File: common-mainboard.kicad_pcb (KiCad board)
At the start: 2 copper layers, 72.4 x 48.3 mm, 82 parts, among them J1 SIM_Card, J2 RSP-122811-01, J3 Conn_01x02_Female, Q1 DTC043ZEB, Q2 DTC043ZEB, Q3 DTC043ZEB, SW1 SW_Push, SW2 SW_Push, U1 ATSAMD21J18A-M, U10 STC3100IQT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

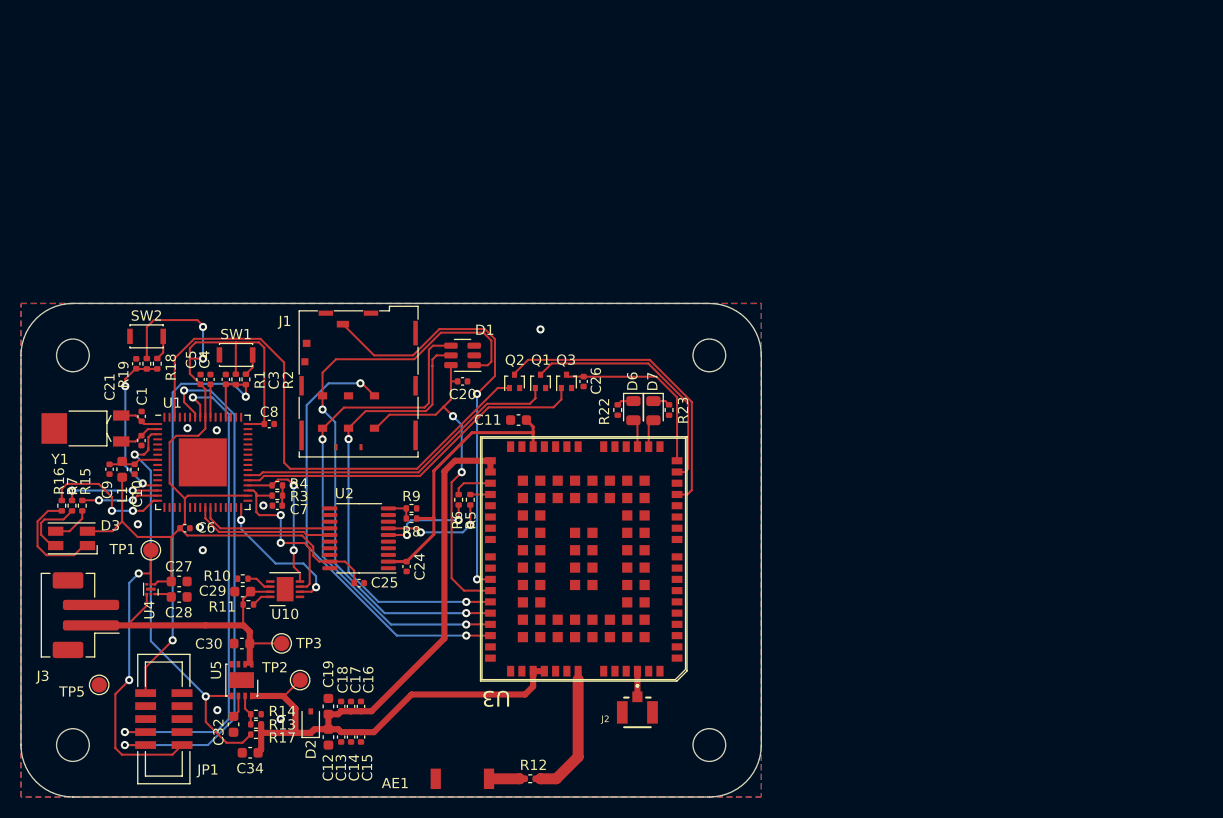
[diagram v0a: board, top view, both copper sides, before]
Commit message: eg915u: modified page layout, added USB upgrade support (sch + pcb)
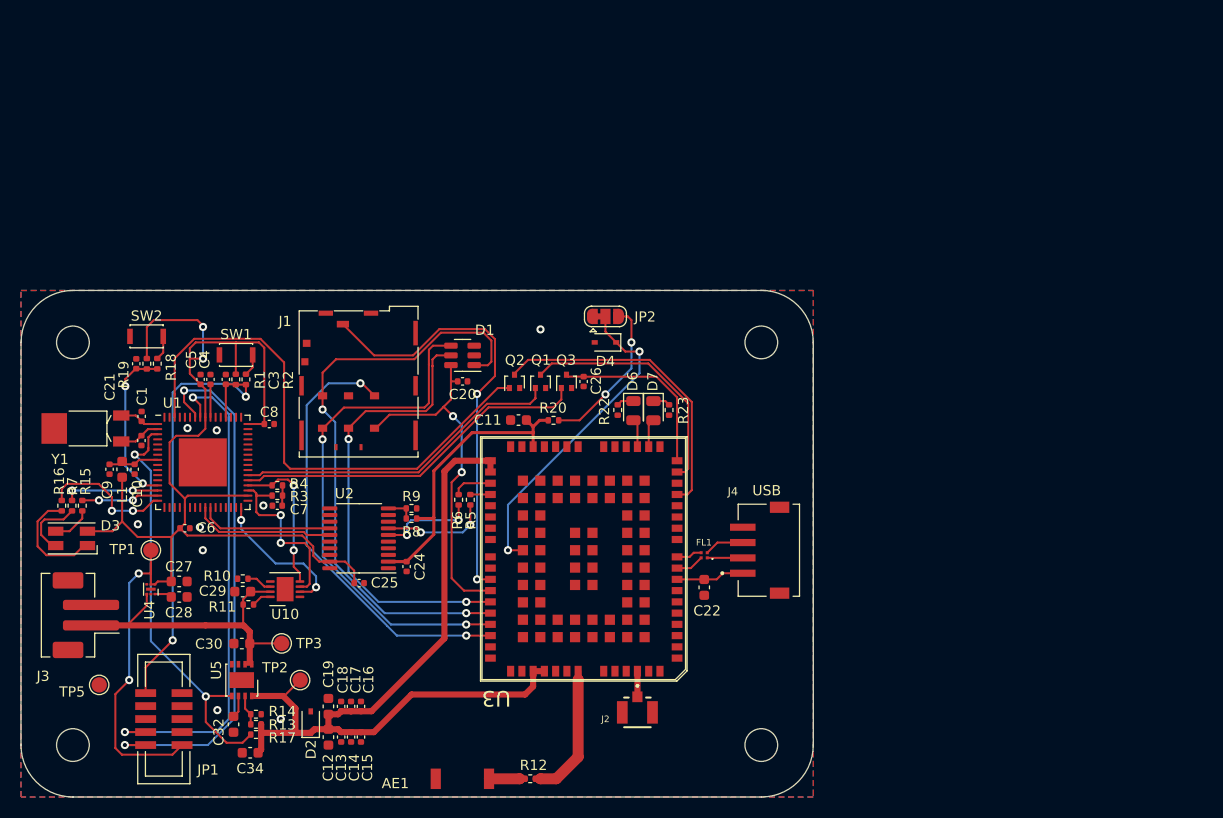
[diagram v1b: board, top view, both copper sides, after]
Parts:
- added C22: 1uF_10V, Capacitor_SMD:C_0603_1608Metric, F.Cu at (137.9, 130.6)
- added D4: SD05_SOD323, Diode_SMD:D_SOD-323, F.Cu at (128.3, 106.7)
- added FL1: DLM0NSN900HY2D, DLM0NSN900HY2D:FIL_DLM0NSN900HY2D, F.Cu at (137.9, 127.5)
- added J4: S4B-ZR-SM4A-TF(LF)(SN), S4B-ZR-SM4A-TF_LF__SN_:JST_S4B-ZR-SM4A-TF(LF)(SN), F.Cu at (141.7, 127.0)
- added JP2: SolderJumper_3_Bridged12, Jumper:SolderJumper-3_P1.3mm_Bridged12_RoundedPad1.0x1.5mm, F.Cu at (128.3, 104.1)
- added R20: 4k7, Resistor_SMD:R_0402_1005Metric, F.Cu at (123.2, 114.3)
- moved H3 5.24 mm to (143.5, 106.7)
- moved H2 5.08 mm to (143.5, 146.1)
- moved H4 1.27 mm to (76.2, 106.7)
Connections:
- U3 pad 10: unconnected-(U3-Pad10) -> Net-(FL1-Pad3)
- U3 pad 75: unconnected-(U3-Pad75) -> USB_BOOT
- U3 pad 8: unconnected-(U3-Pad8) -> USB_VBUS
- U3 pad 9: unconnected-(U3-Pad9) -> Net-(FL1-Pad2)
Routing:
- net USB_BOOT: track 0.00 -> 31.8 mm, vias 0 -> 2
- net Net-(JP2-Pad3): track 0.00 -> 15.3 mm, vias 0 -> 2
- net USB_VBUS: track 0.00 -> 6.67 mm
- net USB_DM: track 0.00 -> 3.88 mm
- net USB_DP: track 0.00 -> 3.47 mm
- net Net-(FL1-Pad2): track 0.00 -> 2.77 mm
- net Net-(FL1-Pad3): track 0.00 -> 2.52 mm
- net VDD_EXT: track 27.8 -> 29.5 mm
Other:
- board size 72.4 x 48.3 mm -> 77.5 x 49.5 mm
- board text added: "USB"

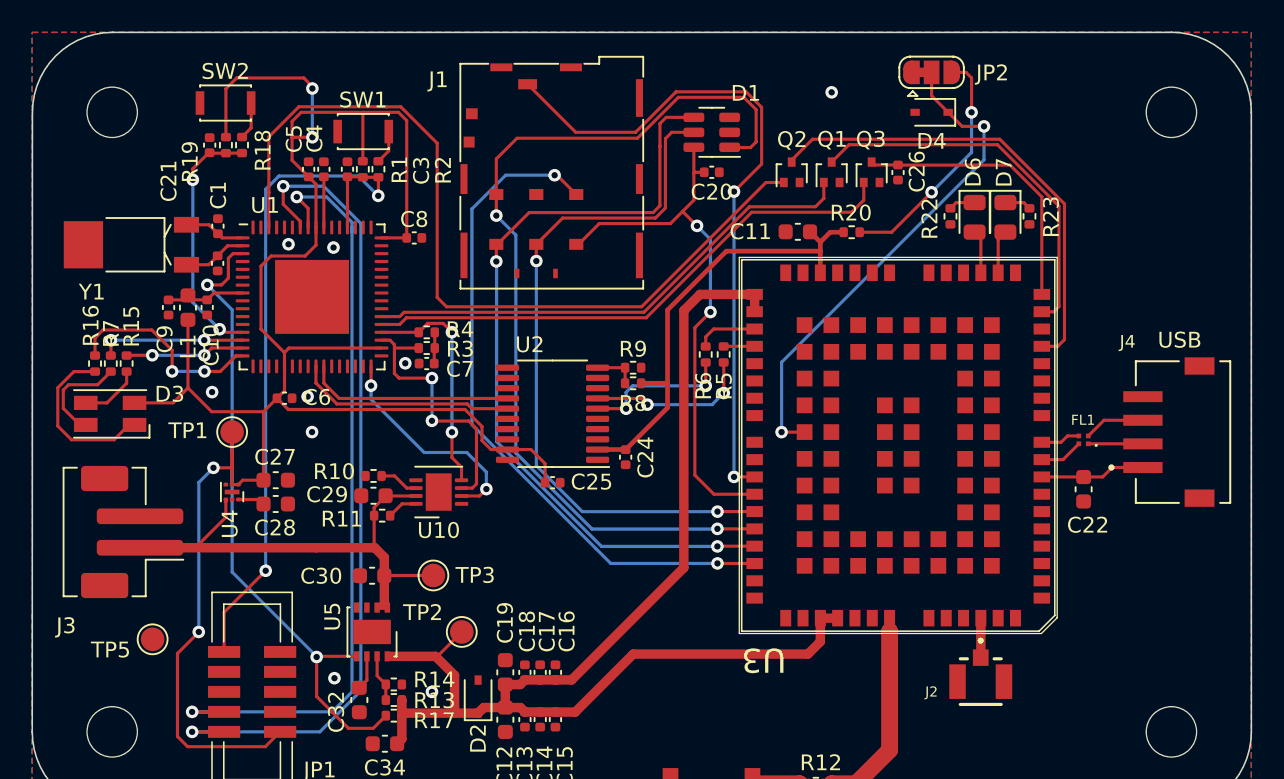
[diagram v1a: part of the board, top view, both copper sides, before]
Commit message: added UART flow control pins CTS and RTS
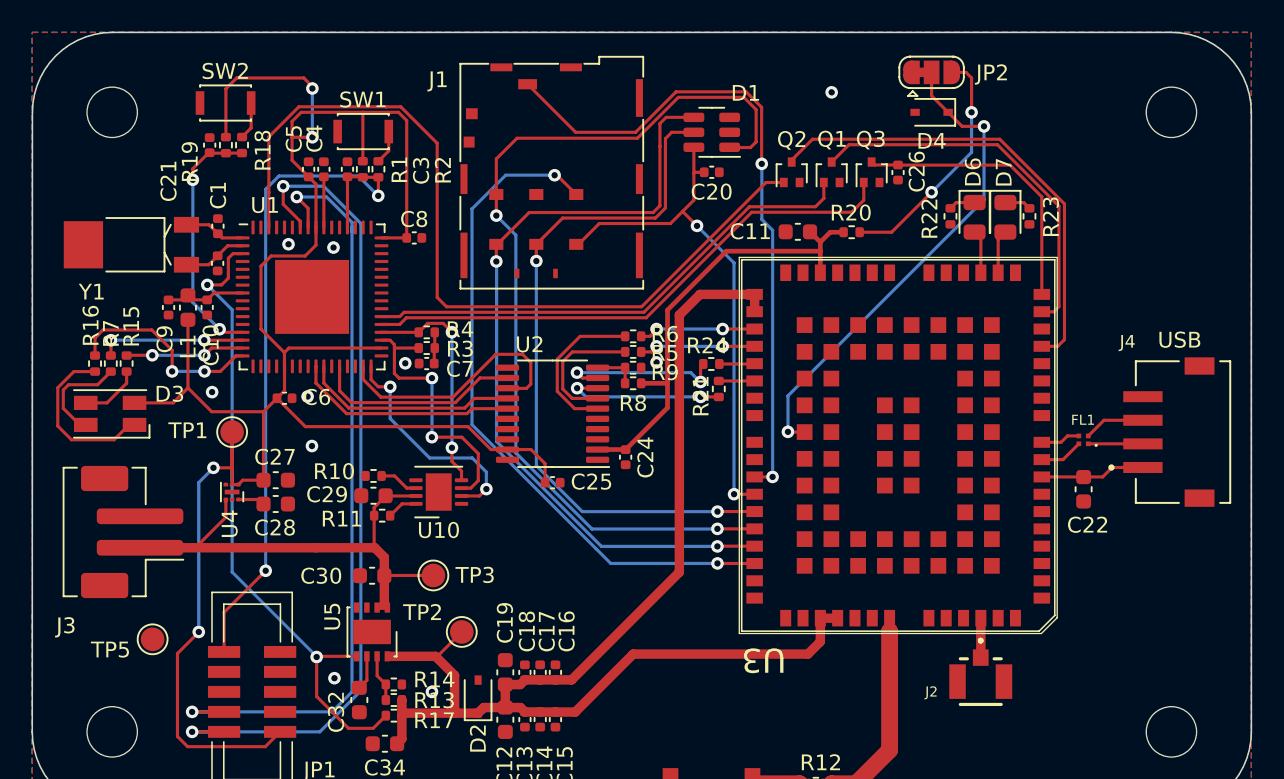
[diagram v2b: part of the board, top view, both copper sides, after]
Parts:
- added R21: 0R, Resistor_SMD:R_0402_1005Metric, F.Cu at (114.7, 124.3)
- added R24: 0R, Resistor_SMD:R_0402_1005Metric, F.Cu at (114.3, 122.7)
- moved R5 5.75 mm to (109.3, 121.9), turned to 180 degrees
- moved R6 4.75 mm to (109.3, 120.9), turned to 180 degrees
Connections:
- U1 pad 28: unconnected-(U1-Pad28) -> UC_DCE_CTS
- U1 pad 31: unconnected-(U1-Pad31) -> UC_DCE_RTS
- U2 pad 12: unconnected-(U2-Pad12) -> UC_DCE_CTS
- U2 pad 13: unconnected-(U2-Pad13) -> UC_DCE_RTS
- U2 pad 8: unconnected-(U2-Pad8) -> DCE_RTS
- U2 pad 9: unconnected-(U2-Pad9) -> DCE_CTS
- U3 pad 36: unconnected-(U3-Pad36) -> Net-(U3-Pad36)
- U3 pad 37: unconnected-(U3-Pad37) -> Net-(U3-Pad37)
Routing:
- net UC_DCE_RTS: track 0.00 -> 16.3 mm
- net UC_DCE_CTS: track 0.00 -> 13.2 mm
- net DCE_CTS: track 0.00 -> 10.8 mm, vias 0 -> 2
- net DCE_RTS: track 0.00 -> 10.5 mm, vias 0 -> 2
- net Net-(R5-Pad1): track 1.97 -> 7.40 mm, vias 0 -> 2
- net Net-(R6-Pad1): track 3.92 -> 7.50 mm, vias 0 -> 2
- net Net-(U3-Pad37): track 0.00 -> 2.28 mm
- net Net-(U3-Pad36): track 0.00 -> 2.25 mm
- net DCE_TX: track 10.4 -> 8.43 mm, vias 2 -> 0
- net USIM1_VDD: track 34.9 -> 33.3 mm
- net USIM1_DET: track 43.1 -> 42.5 mm
- net USB_BOOT: track 31.8 -> 31.3 mm
- net +3V3: track 136.0 -> 135.5 mm
- net UC_DCE_TX: track 13.1 -> 13.7 mm
- net DCE_RX: track 9.57 -> 9.97 mm, vias 2 -> 0
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
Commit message: added test point for VDD_EXT
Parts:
- added TP4: VDD_EXT, TestPoint:TestPoint_Pad_D1.5mm, F.Cu at (109.4, 131.4)
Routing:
- net VDD_EXT: track 29.5 -> 35.2 mm
- net GNDREF: vias 10 -> 13
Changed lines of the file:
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@@
   (net 186 "UC_DCE_CTS")
   (net 187 "UC_DCE_RTS")
+  (footprint "TestPoint:TestPoint_Pad_D1.5mm" (layer "F.Cu")
+    (at 109.350602 131.40853)
+    (descr "SMD pad as test Point, diameter 1.5mm")
+    (tags "test point SMD pad")
+    (property "Sheetfile" "lipo-power-supply.kicad_sch")
+    (property "Sheetname" "lipo-power-supply")
+    (attr exclude_from_pos_files)
+    (fp_text reference "TP4" (at 0 2.059945) (layer "F.SilkS")
+      (effects (font (size 1 1) (thickness 0.15)))
+    )
+    (fp_text value "VDD_EXT" (at 0 1.75) (layer "F.Fab")
+      (effects (font (size 1 1) (thickness 0.15)))
+    )
+    (fp_text user "${REFERENCE}" (at 0 -1.65) (layer "F.Fab")
+      (effects (font (size 1 1) (thickness 0.15)))
+    )
+    (fp_circle (center 0 0) (end 0 0.95) (layer "F.SilkS") (width 0.12) (fill none))
+    (fp_circle (center 0 0) (end 1.25 0) (layer "F.CrtYd") (width 0.05) (fill none))
+    (pad "1" smd circle (at 0 0) (size 1.5 1.5) (layers "F.Cu" "F.Mask")
+      (net 19 "VDD_EXT") (pinfunction "1") (pintype "passive"))
+  )
   (footprint "Resistor_SMD:R_0402_1005Metric" (layer "F.Cu")
     (at 120.915065 149.347023)
@@
   (via (at 96.52 143.51) (size 0.8) (drill 0.4) (layers "F.Cu" "B.Cu") (free) (net 2))
   (via (at 88.893866 127.886012) (size 0.8) (drill 0.4) (layers "F.Cu" "B.Cu") (free) (net 2))
+  (via (at 109.645313 126.36262) (size 0.8) (drill 0.4) (layers "F.Cu" "B.Cu") (free) (net 2))
   (via (at 90.263294 115.272692) (size 0.8) (drill 0.4) (layers "F.Cu" "B.Cu") (free) (net 2))
+  (via (at 114.3 119.38) (size 0.8) (drill 0.4) (layers "F.Cu" "B.Cu") (free) (net 2))
   (via (at 88.616178 124.74512) (size 0.8) (drill 0.4) (layers "F.Cu" "B.Cu") (free) (net 2))
+  (via (at 94.076408 112.56816) (size 0.8) (drill 0.4) (layers "F.Cu" "B.Cu") (free) (net 2))
   (via (at 121.92 105.41) (size 0.8) (drill 0.4) (layers "F.Cu" "B.Cu") (net 2))
   (via (at 82.55 124.46) (size 0.8) (drill 0.4) (layers "F.Cu" "B.Cu") (free) (net 2))
@@
   (segment (start 107.046544 128.110177) (end 108.821748 128.110177) (width 0.3) (layer "F.Cu") (net 19))
   (segment (start 111.490312 123.820192) (end 111.490312 119.240652) (width 0.3) (layer "F.Cu") (net 19))
-  (segment (start 108.827325 128.115754) (end 111.490312 125.452767) (width 0.3) (layer "F.Cu") (net 19))
   (segment (start 121.2 115.50329) (end 121.2 114.927745) (width 0.3) (layer "F.Cu") (net 19))
   (segment (start 109.933711 124.018434) (end 109.813685 123.898408) (width 0.3) (layer "F.Cu") (net 19))
+  (segment (start 108.827325 128.115754) (end 108.837885 128.105194) (width 0.3) (layer "F.Cu") (net 19))
   (segment (start 121.2 114.927745) (end 120.545187 114.272932) (width 0.3) (layer "F.Cu") (net 19))
   (segment (start 111.490312 119.240652) (end 115.227674 115.50329) (width 0.3) (layer "F.Cu") (net 19))
+  (segment (start 108.837885 128.105194) (end 111.466221 128.105194) (width 0.3) (layer "F.Cu") (net 19))
   (segment (start 121.2 116.875) (end 121.2 115.50329) (width 0.3) (layer "F.Cu") (net 19))
   (segment (start 111.412096 123.898408) (end 111.490312 123.820192) (width 0.3) (layer "F.Cu") (net 19))
+  (segment (start 109.350602 131.40853) (end 111.490312 129.26882) (width 0.3) (layer "F.Cu") (net 19))
   (segment (start 111.490312 125.452767) (end 111.490312 123.820192) (width 0.3) (layer "F.Cu") (net 19))
   (segment (start 109.813685 123.898408) (end 111.412096 123.898408) (width 0.3) (layer "F.Cu") (net 19))
   (segment (start 121.827745 114.3) (end 121.2 114.927745) (width 0.3) (layer "F.Cu") (net 19))
   (segment (start 115.227674 115.50329) (end 121.2 115.50329) (width 0.3) (layer "F.Cu") (net 19))
+  (segment (start 111.490312 129.26882) (end 111.490312 125.452767) (width 0.3) (layer "F.Cu") (net 19))
   (segment (start 105.626014 144.791793) (end 104.369914 144.791793) (width 0.6) (layer "F.Cu") (net 20))
   (segment (start 99.452509 144.86) (end 97.959126 144.86) (width 0.6) (layer "F.Cu") (net 20))

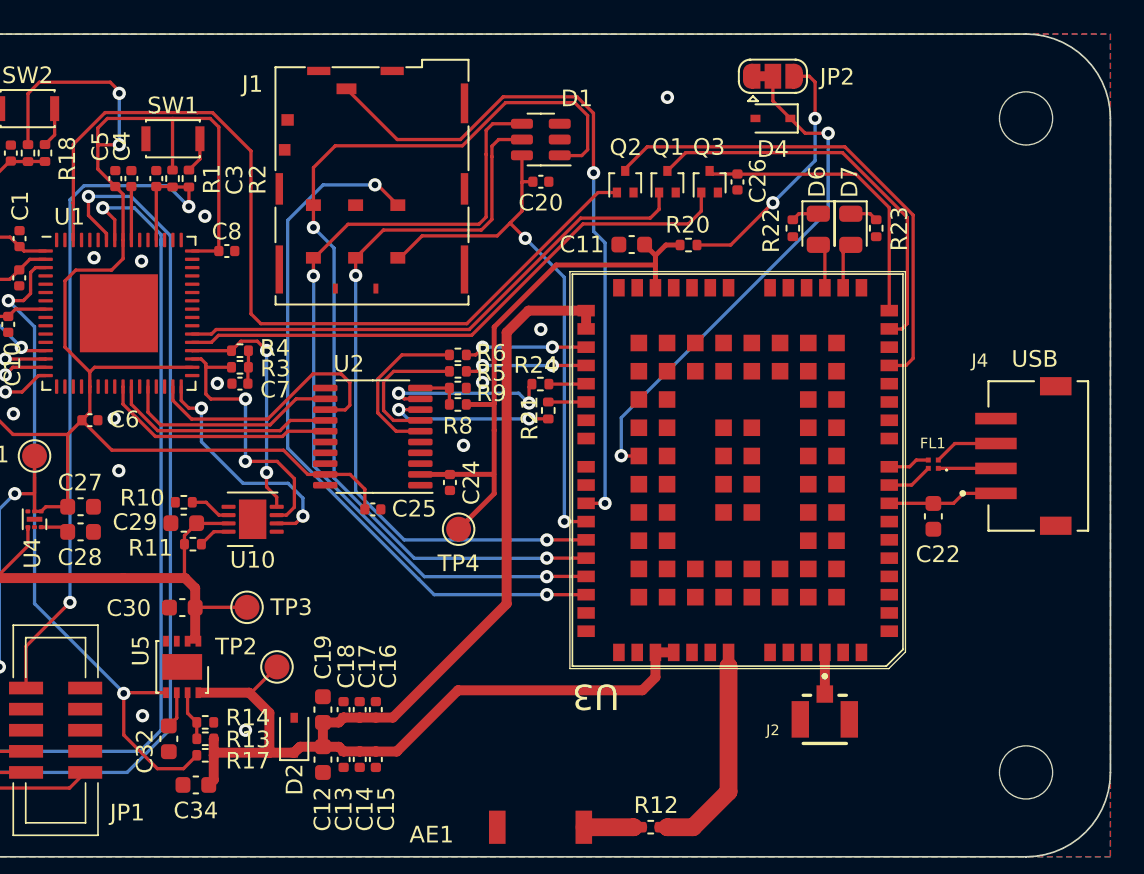
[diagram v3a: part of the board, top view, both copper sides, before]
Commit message: 3.8V LDO: added output enable control from uc
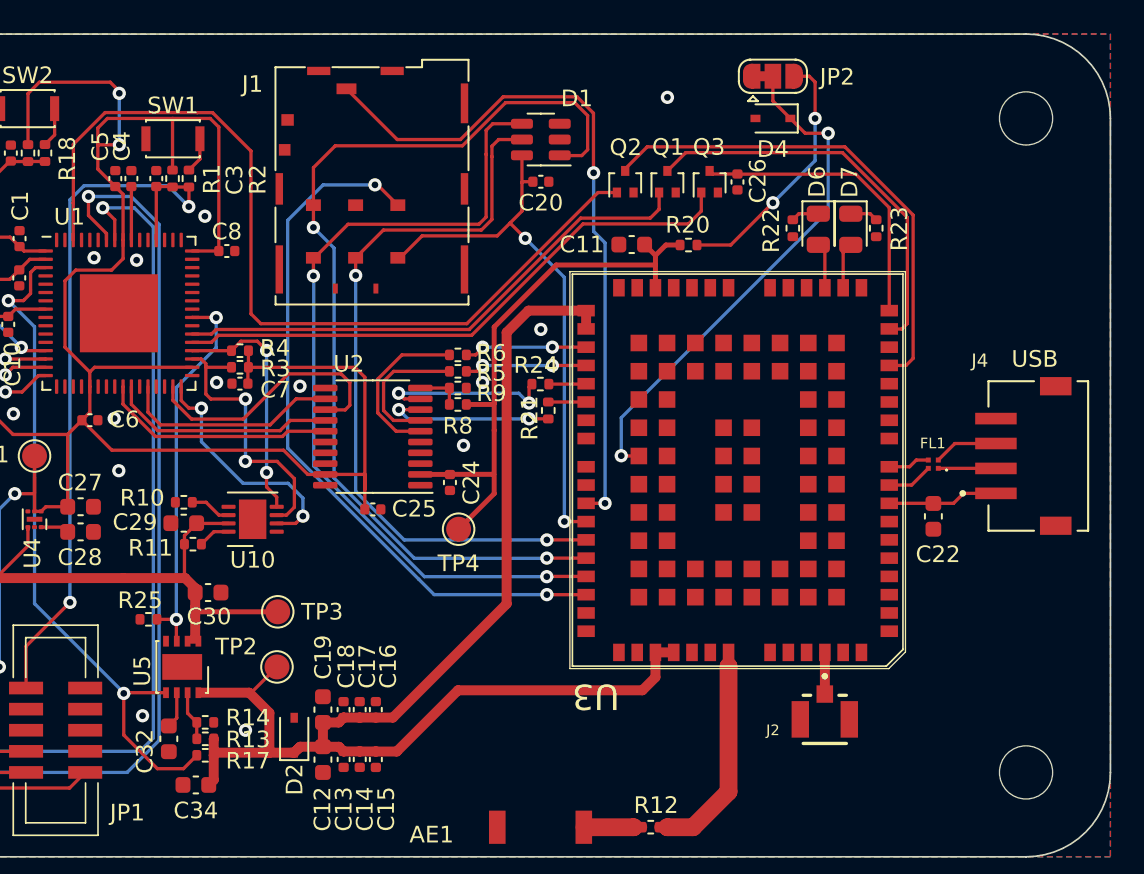
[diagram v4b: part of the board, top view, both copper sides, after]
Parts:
- added R25: 4k7, Resistor_SMD:R_0402_1005Metric, F.Cu at (90.7, 136.8)
- moved TP3 1.87 mm to (98.5, 136.4)
- moved C30 1.80 mm to (94.3, 135.2), turned to 0 degrees
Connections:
- U1 pad 40: unconnected-(U1-Pad40) -> 3.8V_EN
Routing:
- net 3.8V_EN: track 0.00 -> 23.1 mm, vias 0 -> 2
- net +3V3: track 135.5 -> 150.0 mm
- net VBAT: track 37.5 -> 39.4 mm
- net SWD_CLK: track 49.3 -> 48.6 mm
- net SWD_DATA: track 52.5 -> 51.9 mm
- net GNDREF: vias 13 -> 14
